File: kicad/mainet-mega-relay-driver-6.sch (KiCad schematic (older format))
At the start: 10 parts, among them J35 Screw_Terminal_01x03, J89 Conn_01x01_Male, J90 Conn_01x01_Male, K6 SANYOU_SRD_Form_C, Q6 2N3904, U7 4N37

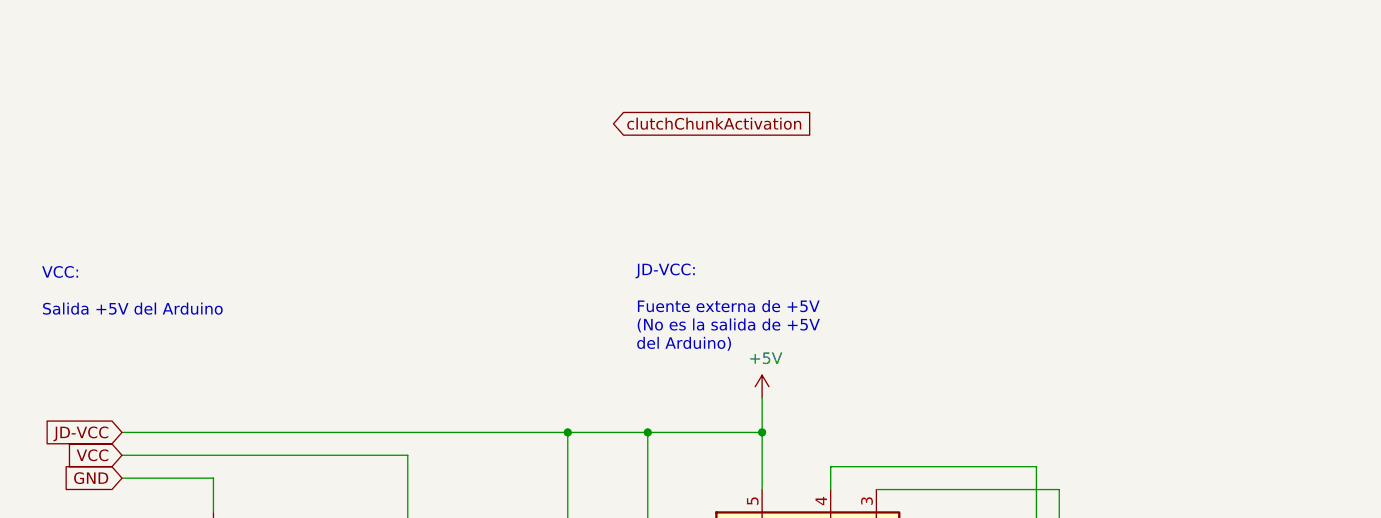
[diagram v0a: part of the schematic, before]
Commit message: KICAD: Actualizar .sch manejadores de relés Agrega alimentación de +5V de dispositivos del lado del Arduino diferente a la salida de +5V del Arduino
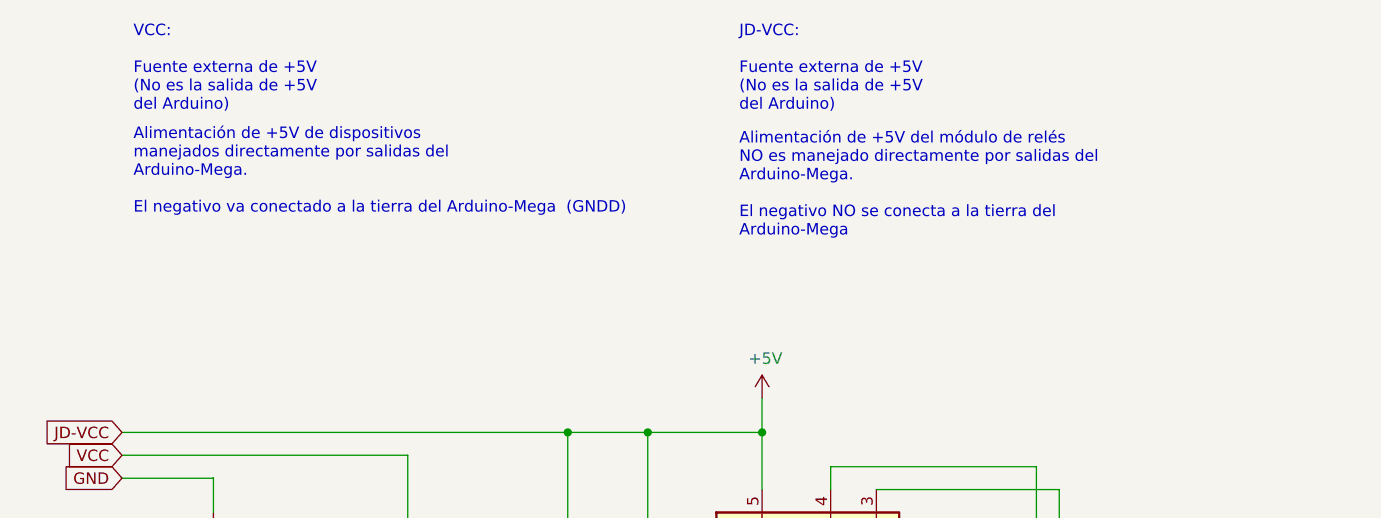
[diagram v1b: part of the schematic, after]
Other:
- note added: "Alimentación de +5V de dispositivos \nmanejados directamente por salidas del \nArduino-Mega.\n\nEl negativo va conectado a la tierra del Arduino-Mega (GNDD)"
- note added: "Alimentación de +5V del módulo de relés \nNO es manejado directamente por salidas del \nArduino-Mega.\n\nEl negativo NO se conecta a la tierra del \nArduino-Mega"
- note added: "VCC:\n\nFuente externa de +5V\n(No es la salida de +5V \ndel Arduino)"
- note removed: "VCC:\n\nSalida +5V del Arduino"
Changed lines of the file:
@@
 Text GLabel 3100 3200 0    50   Input ~ 0
 GND
-Text Notes 5350 2650 0    50   ~ 0
-JD-VCC:\n\nFuente externa de +5V\n(No es la salida de +5V \ndel Arduino)
-Text Notes 2750 2500 0    50   ~ 0
-VCC:\n\nSalida +5V del Arduino
 Text Notes 2900 4450 0    50   ~ 0
 D16-clutchChuckControl
@@
 Text Notes 5550 4950 0    50   ~ 0
 Relay Ground\nNo conectar a la tierra\ndel Arduino Mega\n
-Text GLabel 5250 1650 2    50   Input ~ 0
-clutchChunkActivation
 Text GLabel 9000 3300 2    50   Input ~ 0
 +24V
@@
 Wire Wire Line
 	8700 3300 8700 3750
+Text Notes 5800 1600 0    50   ~ 0
+JD-VCC:\n\nFuente externa de +5V\n(No es la salida de +5V \ndel Arduino)
+Text Notes 3150 1600 0    50   ~ 0
+VCC:\n\nFuente externa de +5V\n(No es la salida de +5V \ndel Arduino)
+Text Notes 3150 2050 0    50   ~ 0
+Alimentación de +5V de dispositivos \nmanejados directamente por salidas del \nArduino-Mega.\n\nEl negativo va conectado a la tierra del Arduino-Mega  (GNDD)
+Text Notes 5800 2150 0    50   ~ 0
+Alimentación de +5V del módulo de relés \nNO es manejado directamente por salidas del \nArduino-Mega.\n\nEl negativo NO se conecta a la tierra del \nArduino-Mega
 $EndSCHEMATC

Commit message: KICAD: Corregir numeración pines Arduino de control de relés
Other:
- note added: "D5-clutchChuckControl"
- note removed: "D16-clutchChuckControl"
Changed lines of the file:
@@
 GND
 Text Notes 2900 4450 0    50   ~ 0
-D16-clutchChuckControl
+D5-clutchChuckControl
 $Comp
 L Connector:Conn_01x01_Male J?
